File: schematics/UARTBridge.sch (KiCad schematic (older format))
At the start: 6 parts, among them U14 CP2102, U17 SP0503BAHT

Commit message: feat: external power circuit schematics
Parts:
- C44, C46: footprint Capacitors_SMD:C_0603 -> Capacitor_SMD:C_0603_1608Metric
- R51: footprint Resistors_SMD:R_0603 -> Resistor_SMD:R_0603_1608Metric
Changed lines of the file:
@@
 F 0 "R51" V 5550 5050 50  0000 C CNN
 F 1 "1K" V 5470 5050 50  0000 C CNN
-F 2 "Resistors_SMD:R_0603" V 5400 5050 50  0001 C CNN
+F 2 "Resistor_SMD:R_0603_1608Metric" V 5400 5050 50  0001 C CNN
 F 3 "" H 5470 5050 50  0001 C CNN
 	1    5470 5050
@@
 F 0 "C46" H 4625 5605 50  0000 L CNN
 F 1 "4.7u" H 4625 5455 50  0000 L CNN
-F 2 "Capacitors_SMD:C_0603" H 4615 5535 50  0001 C CNN
+F 2 "Capacitor_SMD:C_0603_1608Metric" H 4615 5535 50  0001 C CNN
 F 3 "" H 4615 5535 50  0001 C CNN
 	1    4615 5535
@@
 F 0 "C44" H 4205 4605 50  0000 L CNN
 F 1 "4.7u" H 4205 4455 50  0000 L CNN
-F 2 "Capacitors_SMD:C_0603" H 4195 4535 50  0001 C CNN
+F 2 "Capacitor_SMD:C_0603_1608Metric" H 4195 4535 50  0001 C CNN
 F 3 "" H 4195 4535 50  0001 C CNN
 	1    4195 4535

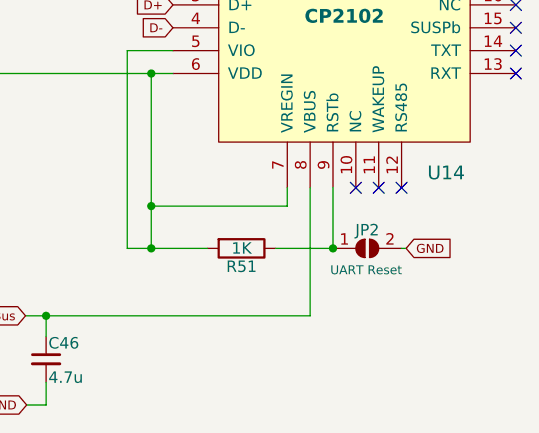
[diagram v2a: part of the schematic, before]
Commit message: feat: UART resets
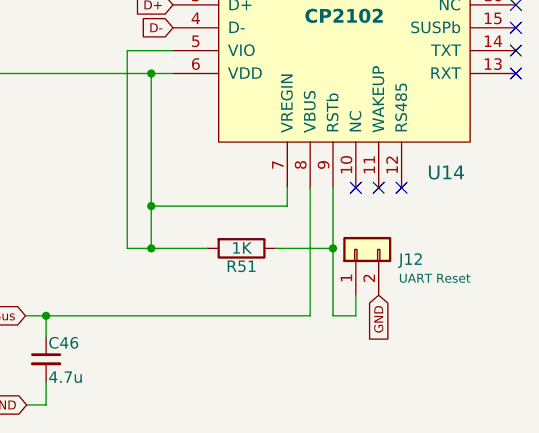
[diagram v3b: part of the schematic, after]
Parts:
- removed JP2: UART Reset, Connectors:GS2, symbol Jumper:SolderJumper_2_Open
- added J12: UART Reset, Connector_PinHeader_2.00mm:PinHeader_1x02_P2.00mm_Vertical, symbol Connector_Generic:Conn_01x02
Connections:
- net GND: now also J12.2 (Pin_2)
- net at R51.1, U14.9 (RSTb): now also J12.1 (Pin_1)
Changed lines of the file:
@@
 Wire Wire Line
 	5075 4865 5075 5050
+Text GLabel 6070 5255 3    39   Input ~ 0
+GND
 $Comp
-L Jumper:SolderJumper_2_Open JP2
-U 1 1 5C9A740E
-P 6020 5050
-F 0 "JP2" H 6020 5130 50  0000 C CNN
-F 1 "UART Reset" H 6015 4955 39  0000 C CNN
-F 2 "Connectors:GS2" H 6020 5050 50  0001 C CNN
-F 3 "~" H 6020 5050 50  0001 C CNN
-	1    6020 5050
-	1    0    0    -1
+L Connector_Generic:Conn_01x02 J12
+U 1 1 5EF5F041
+P 5970 5055
+F 0 "J12" V 5926 4867 50  0000 R CNN
+F 1 "UART Reset" V 5843 4867 39  0000 R CNN
+F 2 "Connector_PinHeader_2.00mm:PinHeader_1x02_P2.00mm_Vertical" H 5970 5055 50  0001 C CNN
+F 3 "~" H 5970 5055 50  0001 C CNN
+	1    5970 5055
+	0    -1   -1   0
 $EndComp
+Wire Wire Line
+	5870 5050 5870 5345
+Wire Wire Line
+	5870 5345 5970 5345
+Wire Wire Line
+	5970 5345 5970 5255
 Connection ~ 5870 5050
-Text GLabel 6190 5050 2    39   Input ~ 0
-GND
-Wire Wire Line
-	6190 5050 6170 5050
 $EndSCHEMATC

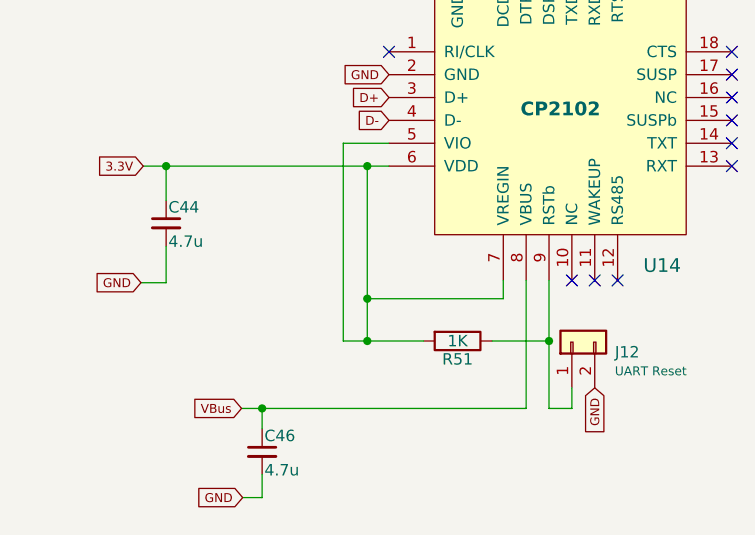
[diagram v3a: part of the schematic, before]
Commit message: feat: added v divider for UART
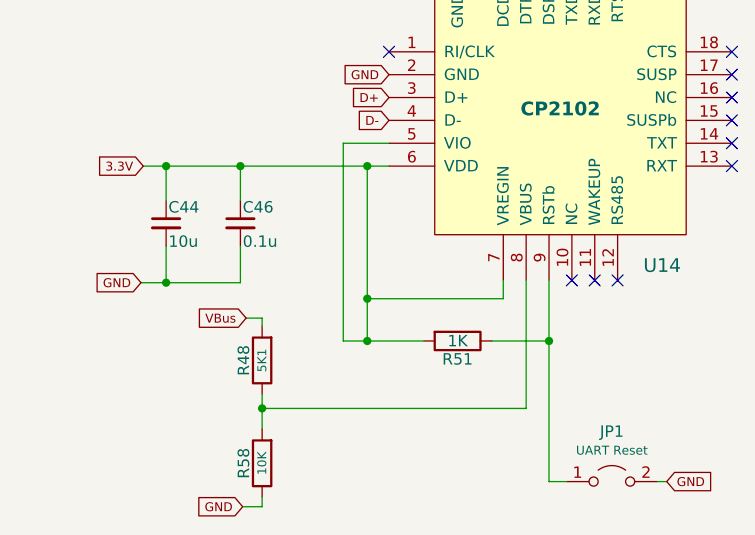
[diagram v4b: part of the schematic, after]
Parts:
- removed J12: UART Reset, Connector_PinHeader_2.00mm:PinHeader_1x02_P2.00mm_Vertical, symbol Connector_Generic:Conn_01x02
- added JP1: UART Reset, Jumper:SolderJumper-2_P1.3mm_Open_RoundedPad1.0x1.5mm, symbol Jumper:Jumper_2_Open
- added R48: 5K1, Resistor_SMD:R_0603_1608Metric, symbol PSLab-rescue:R
- added R58: 10K, Resistor_SMD:R_0603_1608Metric, symbol PSLab-rescue:R
- C44: value 4.7u -> 10u
- C46: value 4.7u -> 0.1u
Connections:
- net 3.3V: now also C46.1
- net GND: now also JP1.2 (B), R58.1
- net VBus: now also R48.2; no longer C46.1, U14.8 (VBUS)
- net at R51.1, U14.9 (RSTb): now also JP1.1 (A)
- new net: R48.1, R58.2, U14.8 (VBUS)
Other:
- moved on the sheet: C46
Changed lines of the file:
@@
 L PSLab-rescue:C_Small C46
 U 1 1 5C5008BB
-P 4615 5535
+P 4520 4535
 AR Path="/5C5008BB" Ref="C46"  Part="1"
 AR Path="/5C4FD460/5C5008BB" Ref="C46"  Part="1"
-F 0 "C46" H 4625 5605 50  0000 L CNN
-F 1 "4.7u" H 4625 5455 50  0000 L CNN
-F 2 "Capacitor_SMD:C_0603_1608Metric" H 4615 5535 50  0001 C CNN
-F 3 "" H 4615 5535 50  0001 C CNN
-	1    4615 5535
+F 0 "C46" H 4530 4605 50  0000 L CNN
+F 1 "0.1u" H 4530 4455 50  0000 L CNN
+F 2 "Capacitor_SMD:C_0603_1608Metric" H 4520 4535 50  0001 C CNN
+F 3 "" H 4520 4535 50  0001 C CNN
+	1    4520 4535
 	1    0    0    -1
 $EndComp
@@
 AR Path="/5C4FD460/5C500F1A" Ref="C44"  Part="1"
 F 0 "C44" H 4205 4605 50  0000 L CNN
-F 1 "4.7u" H 4205 4455 50  0000 L CNN
+F 1 "10u" H 4205 4455 50  0000 L CNN
 F 2 "Capacitor_SMD:C_0603_1608Metric" H 4195 4535 50  0001 C CNN
 F 3 "" H 4195 4535 50  0001 C CNN
@@
 $EndComp
 Wire Wire Line
-	4615 5635 4615 5735
-Wire Wire Line
 	4615 5435 4615 5345
-Wire Wire Line
-	4525 5345 4615 5345
 Wire Wire Line
 	4195 4435 4195 4285
@@
 Wire Wire Line
 	4195 4635 4195 4795
-Text GLabel 4525 5345 0    39   Input ~ 0
+Text GLabel 4545 4950 0    39   Input ~ 0
 VBus
 Connection ~ 4615 5345
@@
 Wire Wire Line
 	2370 3200 2440 3200
-Text GLabel 4530 5735 0    39   Input ~ 0
+Text GLabel 4530 5775 0    39   Input ~ 0
 GND
 Text GLabel 4085 4795 0    39   Input ~ 0
@@
 	4195 4795 4085 4795
 Wire Wire Line
-	4615 5735 4530 5735
-Wire Wire Line
-	4615 5345 5770 5345
-Wire Wire Line
 	5075 4285 5170 4285
 Wire Wire Line
-	4195 4285 5075 4285
+	4195 4285 4520 4285
 Wire Wire Line
 	5075 5050 5320 5050
 Wire Wire Line
 	5075 4865 5075 5050
-Text GLabel 6070 5255 3    39   Input ~ 0
+$Comp
+L PSLab-rescue:R R?
+U 1 1 5F56F11A
+P 4615 5585
+AR Path="/5F56F11A" Ref="R?"  Part="1"
+AR Path="/5C4FD460/5F56F11A" Ref="R58"  Part="1"
+F 0 "R58" V 4695 5585 50  0000 C CNN
+F 1 "10K" V 4615 5585 39  0000 C CNN
+F 2 "Resistor_SMD:R_0603_1608Metric" V 4545 5585 50  0001 C CNN
+F 3 "" H 4615 5585 50  0001 C CNN
+	1    4615 5585
+	-1   0    0    1
+$EndComp
+$Comp
+L PSLab-rescue:R R?
+U 1 1 5F56FABD
+P 4615 5135
+AR Path="/5F56FABD" Ref="R?"  Part="1"
+AR Path="/5C4FD460/5F56FABD" Ref="R48"  Part="1"
+F 0 "R48" V 4695 5135 50  0000 C CNN
+F 1 "5K1" V 4615 5135 39  0000 C CNN
+F 2 "Resistor_SMD:R_0603_1608Metric" V 4545 5135 50  0001 C CNN
+F 3 "" H 4615 5135 50  0001 C CNN
+	1    4615 5135
+	-1   0    0    1
+$EndComp
+Wire Wire Line
+	4615 5285 4615 5345
+Wire Wire Line
+	4545 4950 4615 4950
+Wire Wire Line
+	4615 4950 4615 4985
+Wire Wire Line
+	4530 5775 4615 5775
+Wire Wire Line
+	4615 5775 4615 5735
+Wire Wire Line
+	4615 5345 5770 5345
+Connection ~ 5870 5050
+Text GLabel 6385 5665 2    39   Input ~ 0
 GND
 $Comp
-L Connector_Generic:Conn_01x02 J12
-U 1 1 5EF5F041
-P 5970 5055
-F 0 "J12" V 5926 4867 50  0000 R CNN
-F 1 "UART Reset" V 5843 4867 39  0000 R CNN
-F 2 "Connector_PinHeader_2.00mm:PinHeader_1x02_P2.00mm_Vertical" H 5970 5055 50  0001 C CNN
-F 3 "~" H 5970 5055 50  0001 C CNN
-	1    5970 5055
-	0    -1   -1   0
+L Jumper:Jumper_2_Open JP1
+U 1 1 5F57792C
+P 6145 5665
+F 0 "JP1" H 6145 5884 50  0000 C CNN
+F 1 "UART Reset" H 6145 5801 39  0000 C CNN
+F 2 "Jumper:SolderJumper-2_P1.3mm_Open_RoundedPad1.0x1.5mm" H 6145 5665 50  0001 C CNN
+F 3 "~" H 6145 5665 50  0001 C CNN
+	1    6145 5665
+	1    0    0    -1
 $EndComp
 Wire Wire Line
-	5870 5050 5870 5345
+	5870 5665 5945 5665
 Wire Wire Line
-	5870 5345 5970 5345
+	6385 5665 6345 5665
 Wire Wire Line
-	5970 5345 5970 5255
-Connection ~ 5870 5050
+	5870 5050 5870 5665
+Wire Wire Line
+	4195 4795 4520 4795
+Wire Wire Line
+	4520 4795 4520 4635
+Connection ~ 4195 4795
+Wire Wire Line
+	4520 4435 4520 4285
+Connection ~ 4520 4285
+Wire Wire Line
+	4520 4285 5075 4285
 $EndSCHEMATC

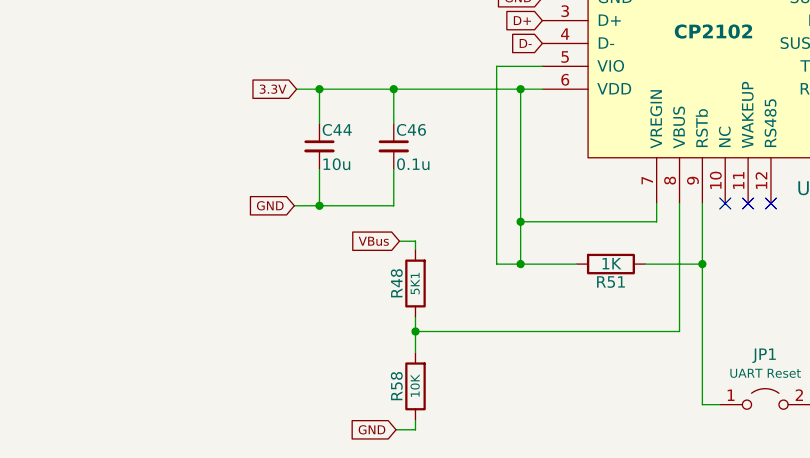
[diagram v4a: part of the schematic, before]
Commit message: refactor: fixed rotation in resistors
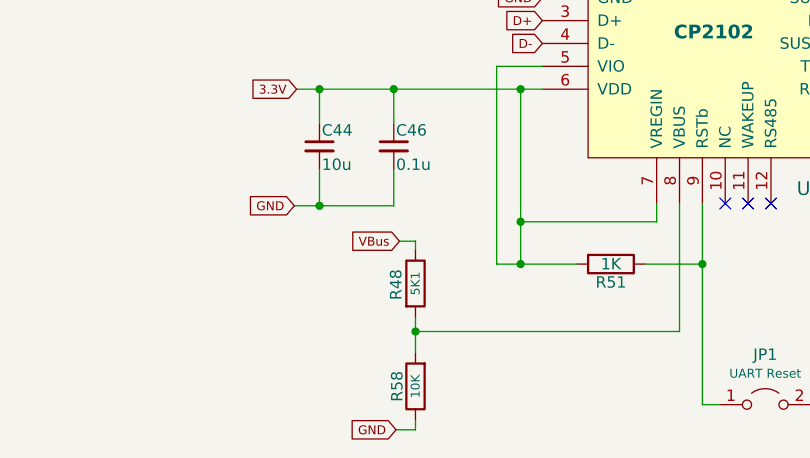
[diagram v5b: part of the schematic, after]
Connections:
- net VBus: now also R48.1; no longer R48.2
- net at R58.2, U14.8 (VBUS): now also R48.2; no longer R48.1
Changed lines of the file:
@@
 AR Path="/5F56FABD" Ref="R?"  Part="1"
 AR Path="/5C4FD460/5F56FABD" Ref="R48"  Part="1"
-F 0 "R48" V 4695 5135 50  0000 C CNN
+F 0 "R48" V 4530 5130 50  0000 C CNN
 F 1 "5K1" V 4615 5135 39  0000 C CNN
 F 2 "Resistor_SMD:R_0603_1608Metric" V 4545 5135 50  0001 C CNN
 F 3 "" H 4615 5135 50  0001 C CNN
 	1    4615 5135
-	-1   0    0    1
+	1    0    0    -1
 $EndComp
 Wire Wire Line

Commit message: refactor: board verification
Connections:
- net VBusSense: now reaches R48.2, R58.2, U14.8 (VBUS)
- net UARTReset: now reaches JP1.1 (A), R51.1, U14.9 (RSTb)
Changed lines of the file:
@@
 Wire Wire Line
 	4520 4285 5075 4285
+Text Label 5870 5130 3    39   ~ 0
+UARTReset
+Text Label 4777 5345 0    39   ~ 0
+VBusSense
+Text Label 4970 4715 1    39   ~ 0
+UARTVIO
+Text Label 5181 4865 0    39   ~ 0
+UARTVREGin
 $EndSCHEMATC

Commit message: feat: bom generator and updated project to support bom generator
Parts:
- C44: Description (none) -> 16V 20%; Mfr No. (none) -> EMK107BC6106MA-T; PartNumber (none) -> EMK107BC6106MA-T; Price (none) -> 0.46
- C46: Description (none) -> 16V 10%; Mfr No. (none) -> C0603C104J4RACTU; PartNumber (none) -> C0603C104J4RACTU; Price (none) -> 0.15
- R48: Description (none) -> 1/16W 5%; Mfr No. (none) -> RR0816P-512-D; PartNumber (none) -> RR0816P-512-D; Price (none) -> 0.1
- R51: Description (none) -> 1/16W 5%; Mfr No. (none) -> RR0816P-102-D; PartNumber (none) -> RR0816P-102-D; Price (none) -> 0.12
- R58: Description (none) -> 1/16W 5%; Mfr No. (none) -> RR0816P-103-D; PartNumber (none) -> RR0816P-103-D; Price (none) -> 0.12
- U14: Description (none) -> QFN-24-1EP_4x4mm_Pitch0.5mm; Mfr No. (none) -> CP2102N-A02-GQFN24; PartNumber (none) -> CP2102N-A02-GQFN24; Price (none) -> 1.35
- U17: Description (none) -> SOT-143; Mfr No. (none) -> SP0503BAHTG; PartNumber (none) -> SP0503BAHTG; Price (none) -> 0.8
- renumbered JP1 to Z6
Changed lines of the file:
@@
 F 1 "CP2102" H 5920 4035 60  0000 C CNB
 F 2 "Housings_DFN_QFN:QFN-24-1EP_4x4mm_Pitch0.5mm" H 5920 4035 60  0001 C CNN
-F 3 "" H 5920 4035 60  0001 C CNN
+F 3 "https://eu.mouser.com/datasheet/2/368/cp2102n-datasheet-1634912.pdf" H 5920 4035 60  0001 C CNN
+F 4 "QFN-24-1EP_4x4mm_Pitch0.5mm" H 5920 4035 50  0001 C CNN "Description"
+F 5 "CP2102N-A02-GQFN24" H 5920 4035 50  0001 C CNN "Mfr No."
+F 6 "CP2102N-A02-GQFN24" H 5920 4035 50  0001 C CNN "PartNumber"
+F 7 "1.35" H 5920 4035 50  0001 C CNN "Price"
 	1    5920 4035
 	1    0    0    -1
@@
 F 1 "SP0503BAHT" H 5925 2585 60  0000 C CNN
 F 2 "TO_SOT_Packages_SMD:SOT-143" H 5925 2335 60  0001 C CNN
-F 3 "" H 5925 2335 60  0001 C CNN
+F 3 "https://eu.mouser.com/datasheet/2/240/Littelfuse_TVS_Diode_Array_SP05_Datasheet.pdf-777043.pdf" H 5925 2335 60  0001 C CNN
+F 4 "SOT-143" H 5925 2335 50  0001 C CNN "Description"
+F 5 "SP0503BAHTG" H 5925 2335 50  0001 C CNN "Mfr No."
+F 6 "SP0503BAHTG" H 5925 2335 50  0001 C CNN "PartNumber"
+F 7 "0.8" H 5925 2335 50  0001 C CNN "Price"
 	1    5925 2335
 	1    0    0    -1
@@
 F 1 "1K" V 5470 5050 50  0000 C CNN
 F 2 "Resistor_SMD:R_0603_1608Metric" V 5400 5050 50  0001 C CNN
-F 3 "" H 5470 5050 50  0001 C CNN
+F 3 "https://eu.mouser.com/datasheet/2/392/susumu_RR_Data_Sheet-1206438.pdf" H 5470 5050 50  0001 C CNN
+F 4 "1/16W 5%" H 5470 5050 50  0001 C CNN "Description"
+F 5 "RR0816P-102-D" H 5470 5050 50  0001 C CNN "Mfr No."
+F 6 "0.12" H 5470 5050 50  0001 C CNN "Price"
+F 7 "RR0816P-102-D" H 5470 5050 50  0001 C CNN "PartNumber"
 	1    5470 5050
 	0    1    1    0
@@
 F 1 "0.1u" H 4530 4455 50  0000 L CNN
 F 2 "Capacitor_SMD:C_0603_1608Metric" H 4520 4535 50  0001 C CNN
-F 3 "" H 4520 4535 50  0001 C CNN
+F 3 "https://eu.mouser.com/datasheet/2/212/KEM_C1002_X7R_SMD-1102033.pdf" H 4520 4535 50  0001 C CNN
+F 4 "16V 10%" H 4520 4535 50  0001 C CNN "Description"
+F 5 "C0603C104J4RACTU" H 4520 4535 50  0001 C CNN "Mfr No."
+F 6 "0.15" H 4520 4535 50  0001 C CNN "Price"
+F 7 "C0603C104J4RACTU" H 4520 4535 50  0001 C CNN "PartNumber"
 	1    4520 4535
 	1    0    0    -1
@@
 F 1 "10u" H 4205 4455 50  0000 L CNN
 F 2 "Capacitor_SMD:C_0603_1608Metric" H 4195 4535 50  0001 C CNN
-F 3 "" H 4195 4535 50  0001 C CNN
+F 3 "https://eu.mouser.com/datasheet/2/396/mlcc02_e-1307760.pdf" H 4195 4535 50  0001 C CNN
+F 4 "16V 20%" H 4195 4535 50  0001 C CNN "Description"
+F 5 "EMK107BC6106MA-T" H 4195 4535 50  0001 C CNN "Mfr No."
+F 6 "0.46" H 4195 4535 50  0001 C CNN "Price"
+F 7 "EMK107BC6106MA-T" H 4195 4535 50  0001 C CNN "PartNumber"
 	1    4195 4535
 	1    0    0    -1
@@
 F 1 "10K" V 4615 5585 39  0000 C CNN
 F 2 "Resistor_SMD:R_0603_1608Metric" V 4545 5585 50  0001 C CNN
-F 3 "" H 4615 5585 50  0001 C CNN
+F 3 "https://eu.mouser.com/datasheet/2/392/susumu_RR_Data_Sheet-1206438.pdf" H 4615 5585 50  0001 C CNN
+F 4 "1/16W 5%" H 4615 5585 50  0001 C CNN "Description"
+F 5 "RR0816P-103-D" H 4615 5585 50  0001 C CNN "Mfr No."
+F 6 "0.12" H 4615 5585 50  0001 C CNN "Price"
+F 7 "RR0816P-103-D" H 4615 5585 50  0001 C CNN "PartNumber"
 	1    4615 5585
 	-1   0    0    1
@@
 F 1 "5K1" V 4615 5135 39  0000 C CNN
 F 2 "Resistor_SMD:R_0603_1608Metric" V 4545 5135 50  0001 C CNN
-F 3 "" H 4615 5135 50  0001 C CNN
+F 3 "https://eu.mouser.com/datasheet/2/392/susumu_RR_Data_Sheet-1206438.pdf" H 4615 5135 50  0001 C CNN
+F 4 "1/16W 5%" H 4615 5135 50  0001 C CNN "Description"
+F 5 "RR0816P-512-D" H 4615 5135 50  0001 C CNN "Mfr No."
+F 6 "0.1" H 4615 5135 50  0001 C CNN "Price"
+F 7 "RR0816P-512-D" H 4615 5135 50  0001 C CNN "PartNumber"
 	1    4615 5135
 	1    0    0    -1
@@
 GND
 $Comp
-L Jumper:Jumper_2_Open JP1
+L Jumper:Jumper_2_Open Z6
 U 1 1 5F57792C
 P 6145 5665
-F 0 "JP1" H 6145 5884 50  0000 C CNN
+F 0 "Z6" H 6145 5884 50  0000 C CNN
 F 1 "UART Reset" H 6145 5801 39  0000 C CNN
 F 2 "Jumper:SolderJumper-2_P1.3mm_Open_RoundedPad1.0x1.5mm" H 6145 5665 50  0001 C CNN

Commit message: refactor: corrected IC annotation order
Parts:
- U15: renamed from U14; value CP2102 -> CP2102N; footprint Housings_DFN_QFN:QFN-24-1EP_4x4mm_Pitch0.5mm -> Package_DFN_QFN:QFN-24-1EP_4x4mm_P0.5mm_EP2.6x2.6mm
- U16: renamed from U17; footprint TO_SOT_Packages_SMD:SOT-143 -> Package_TO_SOT_SMD:SOT-143
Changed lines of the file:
@@
 $EndDescr
 $Comp
-L PSLab:CP2102 U14
+L PSLab:CP2102 U15
 U 1 1 5C4FE1DE
 P 5920 4035
-F 0 "U14" H 6365 3350 60  0000 C CNN
-F 1 "CP2102" H 5920 4035 60  0000 C CNB
-F 2 "Housings_DFN_QFN:QFN-24-1EP_4x4mm_Pitch0.5mm" H 5920 4035 60  0001 C CNN
+F 0 "U15" H 6365 3350 60  0000 C CNN
+F 1 "CP2102N" H 5920 4035 60  0000 C CNB
+F 2 "Package_DFN_QFN:QFN-24-1EP_4x4mm_P0.5mm_EP2.6x2.6mm" H 5920 4035 60  0001 C CNN
 F 3 "https://eu.mouser.com/datasheet/2/368/cp2102n-datasheet-1634912.pdf" H 5920 4035 60  0001 C CNN
 F 4 "QFN-24-1EP_4x4mm_Pitch0.5mm" H 5920 4035 50  0001 C CNN "Description"
@@
 NoConn ~ 5970 4785
 $Comp
-L PSLab:SP0503BAHT U17
+L PSLab:SP0503BAHT U16
 U 1 1 5C4FEC85
 P 5925 2335
-F 0 "U17" H 5925 2085 60  0000 C CNN
+F 0 "U16" H 5925 2085 60  0000 C CNN
 F 1 "SP0503BAHT" H 5925 2585 60  0000 C CNN
-F 2 "TO_SOT_Packages_SMD:SOT-143" H 5925 2335 60  0001 C CNN
+F 2 "Package_TO_SOT_SMD:SOT-143" H 5925 2335 60  0001 C CNN
 F 3 "https://eu.mouser.com/datasheet/2/240/Littelfuse_TVS_Diode_Array_SP05_Datasheet.pdf-777043.pdf" H 5925 2335 60  0001 C CNN
 F 4 "SOT-143" H 5925 2335 50  0001 C CNN "Description"
@@
 P 4520 4535
 AR Path="/5C5008BB" Ref="C46"  Part="1"
-AR Path="/5C4FD460/5C5008BB" Ref="C46"  Part="1"
-F 0 "C46" H 4530 4605 50  0000 L CNN
+AR Path="/5C4FD460/5C5008BB" Ref="C43"  Part="1"
+F 0 "C43" H 4530 4605 50  0000 L CNN
 F 1 "0.1u" H 4530 4455 50  0000 L CNN
 F 2 "Capacitor_SMD:C_0603_1608Metric" H 4520 4535 50  0001 C CNN
@@
 F 7 "C0603C104J4RACTU" H 4520 4535 50  0001 C CNN "PartNumber"
 	1    4520 4535
-	1    0    0    -1
-$EndComp
-$Comp
-L PSLab-rescue:C_Small C44
-U 1 1 5C500F1A
-P 4195 4535
-AR Path="/5C500F1A" Ref="C44"  Part="1"
-AR Path="/5C4FD460/5C500F1A" Ref="C44"  Part="1"
-F 0 "C44" H 4205 4605 50  0000 L CNN
-F 1 "10u" H 4205 4455 50  0000 L CNN
-F 2 "Capacitor_SMD:C_0603_1608Metric" H 4195 4535 50  0001 C CNN
-F 3 "https://eu.mouser.com/datasheet/2/396/mlcc02_e-1307760.pdf" H 4195 4535 50  0001 C CNN
-F 4 "16V 20%" H 4195 4535 50  0001 C CNN "Description"
-F 5 "EMK107BC6106MA-T" H 4195 4535 50  0001 C CNN "Mfr No."
-F 6 "0.46" H 4195 4535 50  0001 C CNN "Price"
-F 7 "EMK107BC6106MA-T" H 4195 4535 50  0001 C CNN "PartNumber"
-	1    4195 4535
 	1    0    0    -1
 $EndComp
@@
 Text Label 5181 4865 0    39   ~ 0
 UARTVREGin
+$Comp
+L PSLab-rescue:C_Small C44
+U 1 1 5C500F1A
+P 4195 4535
+AR Path="/5C500F1A" Ref="C44"  Part="1"
+AR Path="/5C4FD460/5C500F1A" Ref="C44"  Part="1"
+F 0 "C44" H 4205 4605 50  0000 L CNN
+F 1 "10u" H 4205 4455 50  0000 L CNN
+F 2 "Capacitor_SMD:C_0603_1608Metric" H 4195 4535 50  0001 C CNN
+F 3 "https://eu.mouser.com/datasheet/2/396/mlcc02_e-1307760.pdf" H 4195 4535 50  0001 C CNN
+F 4 "16V 20%" H 4195 4535 50  0001 C CNN "Description"
+F 5 "EMK107BC6106MA-T" H 4195 4535 50  0001 C CNN "Mfr No."
+F 6 "0.46" H 4195 4535 50  0001 C CNN "Price"
+F 7 "EMK107BC6106MA-T" H 4195 4535 50  0001 C CNN "PartNumber"
+	1    4195 4535
+	1    0    0    -1
+$EndComp
 $EndSCHEMATC
